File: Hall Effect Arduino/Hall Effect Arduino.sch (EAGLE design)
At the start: 23 parts, among them U1 ATMEGA328P, U2 M5205 5v, X1 Power In, Y1 16MHz

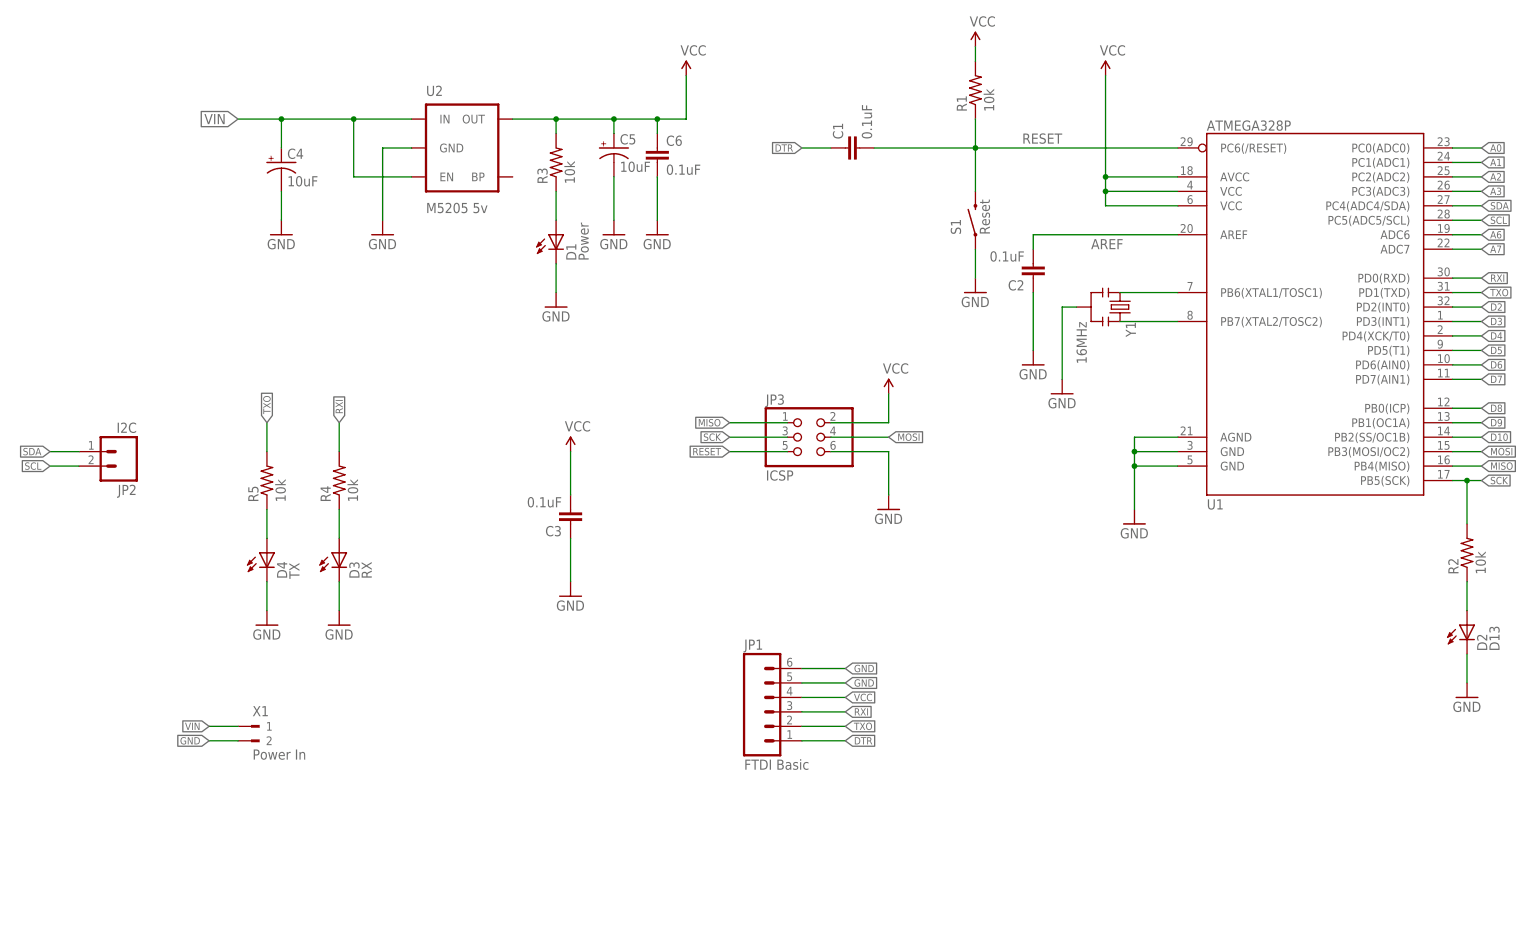
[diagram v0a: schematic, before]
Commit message: Updated with header pins
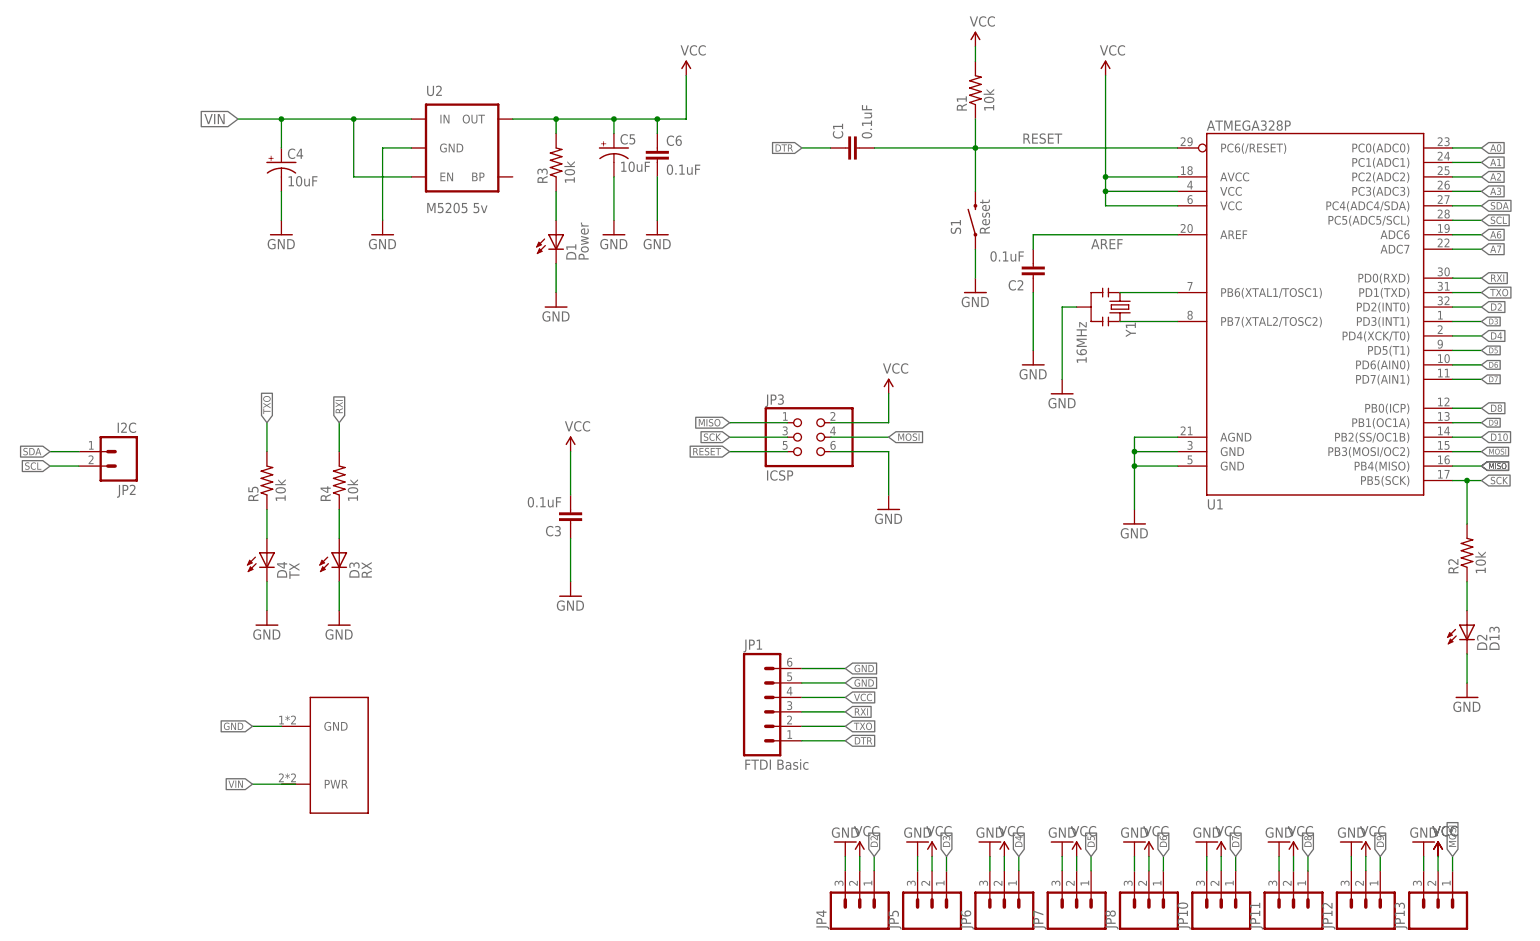
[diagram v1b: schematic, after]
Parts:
- removed X1: Power In, con-weidmueller-sl35:180G-2
- added JP10, JP11, JP12, JP13, JP4, JP5, JP6, JP7, JP8: (no value), SparkFun-Connectors:M03PTH
- added U$1: LSF-SMT, LSF-SMT:LSF-SMT
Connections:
- net D2: now also JP4.1
- net D3: now also JP5.1
- net D4: now also JP6.1
- net D5: now also JP7.1
- net D6: now also JP8.1
- net D7: now also JP10.1
- net D8: now also JP11.1
- net D9: now also JP12.1
- net GND: now also JP10.3, JP11.3, JP12.3, JP13.3, JP4.3, JP5.3, JP6.3, JP7.3, JP8.3, U$1.GND; no longer X1.2
- net MOSI: now also JP13.1
- net VCC: now also JP10.2, JP11.2, JP12.2, JP13.2, JP4.2, JP5.2, JP6.2, JP7.2, JP8.2
- net VIN: no longer X1.1

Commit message: Updated with final board for production.
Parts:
- removed JP2: I2C, SparkFun-Connectors:M02PTH
- added I2C: (no value), SparkFun-Connectors:M03PTH
- renumbered JP10 to 7, JP11 to 8, JP12 to 9, JP13 to 10, JP4 to 2, JP5 to 3, JP6 to 4, JP7 to 5, JP8 to 6
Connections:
- net D10: now also 10.1
- net GND: now also I2C.3
- net MOSI: no longer 10.1
- net SCL: now also I2C.2; no longer JP2.2
- net SDA: now also I2C.1; no longer JP2.1
- net VIN: now also U$1.PWR
